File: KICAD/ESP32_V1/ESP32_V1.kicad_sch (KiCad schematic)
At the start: 24 parts

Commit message: Progress ESP32 V1 KiCad PCB design
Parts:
- added J_ADC_Header1: ADC_Header, ESP32_V1:PinHeader_1x08_P2.54mm_Vertical, symbol Connector_Generic:Conn_01x08
- added J_DS2413: OneWire_DS2413_Breakout, Connector_PinSocket_2.54mm:PinSocket_1x04_P2.54mm_Vertical, symbol Connector_Generic:Conn_01x04
- added J_Port_Header1: Port_Header, ESP32_V1:PinHeader_1x08_P2.54mm_Vertical, symbol Connector_Generic:Conn_01x08
- added R11, R12: 4K7, ESP32_V1:R_Axial_DIN0204_L3.6mm_D1.6mm_P2.54mm_Vertical, symbol Device:R
- added SEL_D26: LOOP_B / DS2413_PIOB, ESP32_V1:PinHeader_1x03_P2.54mm_Vertical, symbol Jumper:Jumper_3_Open
- added SEL_D33: DS2413_PIOA / LOOP_A, ESP32_V1:PinHeader_1x03_P2.54mm_Vertical, symbol Jumper:Jumper_3_Open
- added TP1: TestPoint, ESP32_V1:TestPoint_THTPad_D1.5mm_Drill0.7mm, symbol Connector:TestPoint
- C_FB1: footprint (none) -> ESP32_V1:C_Disc_D4.7mm_W2.5mm_P5.00mm
- JP_External_5V1: value LOCAL_LOOP_DEFAULT_OPEN -> Enable_EXT_5V; footprint (none) -> ESP32_V1:PinHeader_1x02_P2.54mm_Vertical
- JP_UART_LOOP2: value LOCAL_LOOP_DEFAULT_OPEN -> Enable_Uart_Loop2; footprint (none) -> ESP32_V1:PinHeader_1x02_P2.54mm_Vertical
- J_AUTO1, J_UART2: footprint (none) -> ESP32_V1:TerminalBlock_Phoenix_MPT-0,5-3-2.54_1x03_P2.54mm_Horizontal
- J_DUT_L1, J_DUT_R1: footprint (none) -> ESP32_V1:PinSocket_1x19_P2.54mm_Vertical
- J_External_PWR1: footprint (none) -> ESP32_V1:TerminalBlock_Phoenix_MPT-0,5-2-2.54_1x02_P2.54mm_Horizontal
- J_FLASH1: footprint (none) -> ESP32_V1:PinSocket_1x06_P2.54mm_Vertical
- J_Grove_I2C1: footprint (none) -> ESP32_V1:Grove_1x04_P2mm(SEEED_110990030)
- J_ONEWIRE1: renamed from J?_OneWire1; footprint (none) -> ESP32_V1:TerminalBlock_Phoenix_MPT-0,5-3-2.54_1x03_P2.54mm_Horizontal
- R1: renamed from R_UART1; footprint (none) -> ESP32_V1:R_Axial_DIN0204_L3.6mm_D1.6mm_P2.54mm_Vertical
- R2: renamed from R_UART2; footprint (none) -> ESP32_V1:R_Axial_DIN0204_L3.6mm_D1.6mm_P2.54mm_Vertical
- R3: renamed from R_LOOP_A1; footprint (none) -> ESP32_V1:R_Axial_DIN0204_L3.6mm_D1.6mm_P2.54mm_Vertical
- R4: renamed from R_LOOP_B1; footprint (none) -> ESP32_V1:R_Axial_DIN0204_L3.6mm_D1.6mm_P2.54mm_Vertical
- R5: renamed from R_PWM1; footprint (none) -> ESP32_V1:R_Axial_DIN0204_L3.6mm_D1.6mm_P2.54mm_Vertical
- R6: renamed from R_1W1; value 4k7 -> 2K2; footprint (none) -> ESP32_V1:R_Axial_DIN0204_L3.6mm_D1.6mm_P2.54mm_Vertical
- R7: renamed from R_I2C_FB1; footprint (none) -> ESP32_V1:R_Axial_DIN0204_L3.6mm_D1.6mm_P2.54mm_Vertical
- R8: renamed from R_I2C_LOOP1; footprint (none) -> ESP32_V1:R_Axial_DIN0204_L3.6mm_D1.6mm_P2.54mm_Vertical
- SEL_D35: value Jumper_3_Open -> I2C_INT / UART1; footprint (none) -> ESP32_V1:PinHeader_1x03_P2.54mm_Vertical
- U_1W1, U_1W2: footprint (none) -> ESP32_V1:TO-92_Inline
- U_I2C1: footprint (none) -> ESP32_V1:DIP-18_W7.62mm_Socket
- U_SPI1: footprint (none) -> ESP32_V1:DIP-16_W7.62mm_Socket
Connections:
- net 3V3: now also R11.1, R12.1
- net D13_ONEWIRE_DQ: now also J_DS2413.3 (Pin_3)
- net D25_LOOP_B_OUT: now also SEL_D26.1 (A); no longer R4.2
- net D26_LOOP_B_IN: now also R4.2; no longer R4.1
- net D32_LOOP_A_OUT: now also SEL_D33.1 (A); no longer R3.2
- net D33_LOOP_A_IN: now also R3.2; no longer R3.1
- net D34_ADC_IN: now also J_ADC_Header1.1 (Pin_1), TP1.1
- net GND: now also J_DS2413.4 (Pin_4)
- net I2C_GP0: now also J_Port_Header1.1 (Pin_1)
- net I2C_GP1: now also J_Port_Header1.2 (Pin_2)
- net I2C_GP2: now also J_Port_Header1.3 (Pin_3)
- net at U_I2C1.13 (GP3): now also J_Port_Header1.4 (Pin_4)
- net at U_I2C1.14 (GP4): now also J_Port_Header1.5 (Pin_5)
- net at U_I2C1.15 (GP5): now also J_Port_Header1.6 (Pin_6)
- net at U_I2C1.16 (GP6): now also J_Port_Header1.7 (Pin_7)
- net at U_I2C1.17 (GP7): now also J_Port_Header1.8 (Pin_8)
- net at U_SPI1.2 (CH1): now also J_ADC_Header1.2 (Pin_2)
- net at U_SPI1.3 (CH2): now also J_ADC_Header1.3 (Pin_3)
- net at U_SPI1.4 (CH3): now also J_ADC_Header1.4 (Pin_4)
- net at U_SPI1.5 (CH4): now also J_ADC_Header1.5 (Pin_5)
- net at U_SPI1.6 (CH5): now also J_ADC_Header1.6 (Pin_6)
- net at U_SPI1.7 (CH6): now also J_ADC_Header1.7 (Pin_7)
- net at U_SPI1.8 (CH7): now also J_ADC_Header1.8 (Pin_8)
- new net: R3.1, SEL_D33.2 (C)
- new net: R4.1, SEL_D26.2 (C)
- new net DS2413_PIOA: J_DS2413.2 (Pin_2), R11.2, SEL_D33.3 (B)
- new net DS2413_PIOB: J_DS2413.1 (Pin_1), R12.2, SEL_D26.3 (B)
- no-connect marks 24 -> 12
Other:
- note added: "DS2413_PIOA ── R? 470R ── DS2413_FB_A DS2413_PIOB ── R? 470R ── DS2413_FB_B"
- note added: "I2C MCP23008 + GROVE I2C Extension"
- note added: "I’d retain R3 and R4, relocate them to the common paths, and remove R9 and R10."
- note added: "LoopBack Test Selectors - GPIO LOOPBACKS / DS2413 Breakout"
- note added: "ONEWIRE - DS2413 Breakout"
- note added: "ONEWIRE - TWO DS18B20 + External Option"
- note added: "R? 4.7k: 3V3 → DS2413_PIOA R? 4.7k: 3V3 → DS2413_PIOB"
- note added: "R_DS2413_PUA R_DS2413_PUB"
- note removed: "GPIO LOOPBACKS"
- note removed: "I2C MCP23008 (0x20)"
- note removed: "ONEWIRE - TWO POWERED DEVICES"
- moved on the sheet: C_FB1, J_FLASH1, J_Grove_I2C1, J_ONEWIRE1, R3, R4, R5, R6, R7, R8, U_1W1, U_1W2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

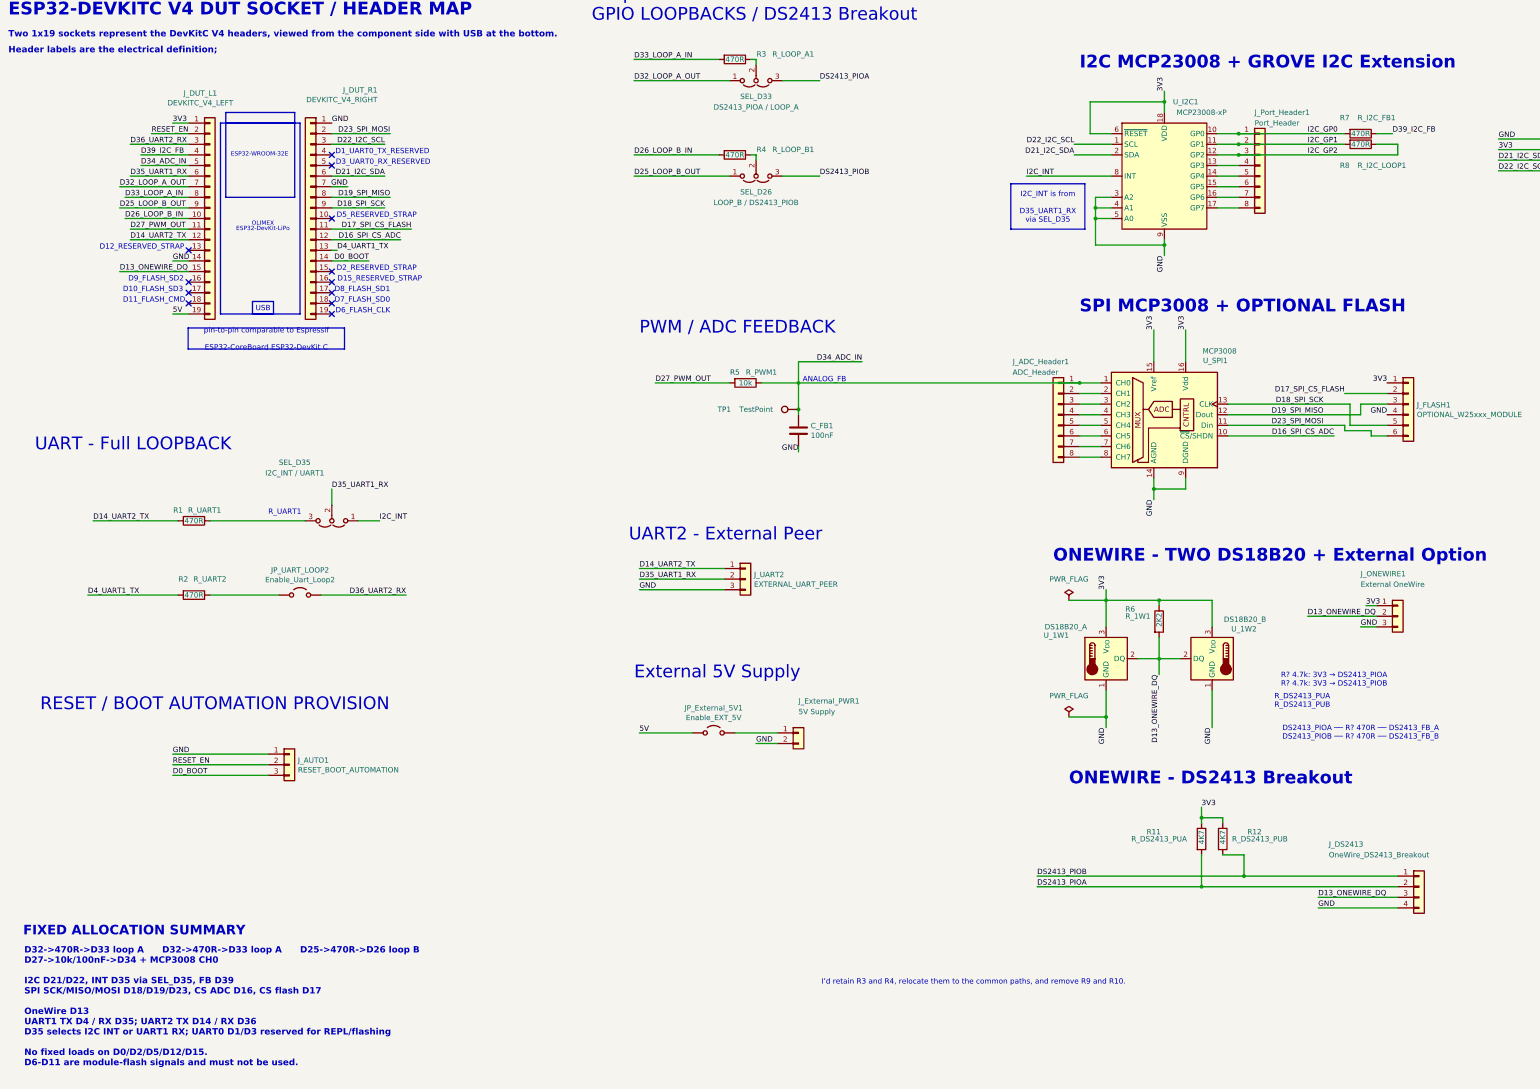
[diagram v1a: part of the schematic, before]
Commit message: Finalize ESP32_V1 v1.0 build documentation
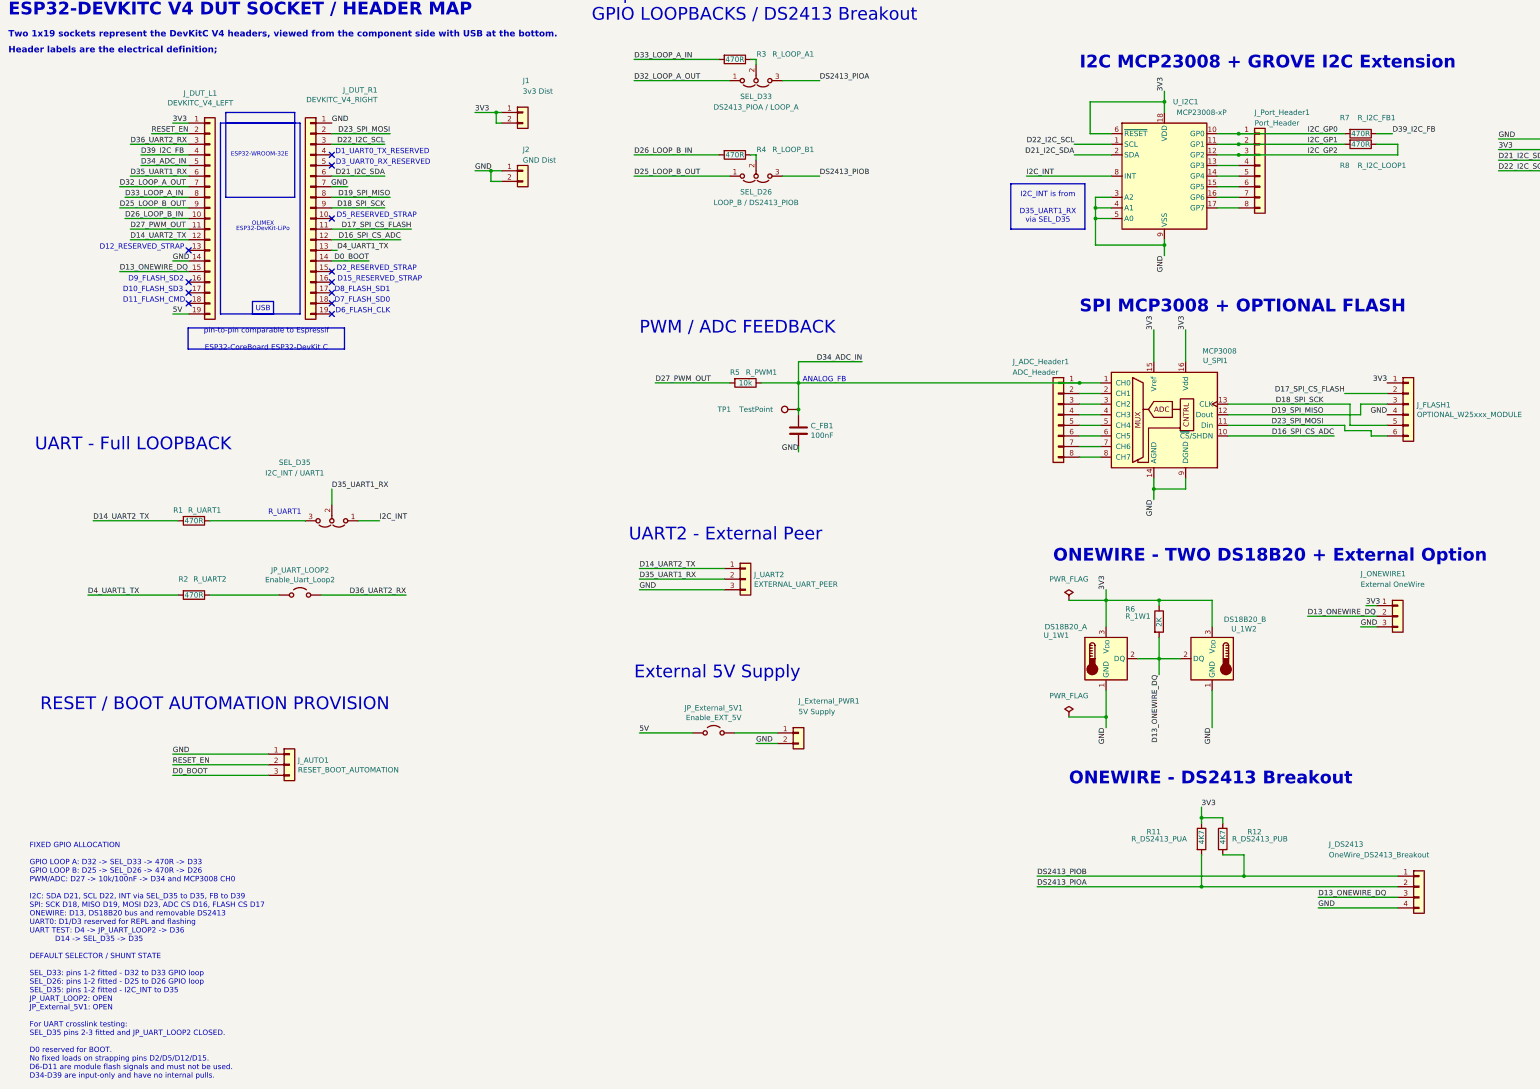
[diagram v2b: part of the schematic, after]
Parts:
- added J1: 3v3 Dist, ESP32_V1:PinHeader_1x02_P2.54mm_Vertical, symbol Connector_Generic:Conn_01x02
- added J2: GND Dist, ESP32_V1:PinHeader_1x02_P2.54mm_Vertical, symbol Connector_Generic:Conn_01x02
- R6: value 2K2 -> 2K
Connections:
- net 3V3: now also J1.1 (Pin_1), J1.2 (Pin_2)
- net GND: now also J2.1 (Pin_1), J2.2 (Pin_2)
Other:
- note added: "FIXED GPIO ALLOCATION GPIO LOOP A: D32 -> SEL_D33 -> 470R -> D33 GPIO LOOP B: D25 -> SEL_D26 -> 470R -> D26 PWM/ADC: D27 -> 10k/100nF -> D34 and MCP3008 CH0 I2C: SDA D21, SCL D22, INT via SEL_D35 to D35, FB to D39 SPI: SCK D18, MISO D19, MOSI D23, ADC CS D16, FLASH CS D17 ONEWIRE: D13, DS18B20 bus and removable DS2413 UART0: D1/D3 reserved for REPL and flashing UART TEST: D4 -> JP_UART_LOOP2 -> D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"
- note removed: "D32->470R->D33 loop A D32->470R->D33 loop A D25->470R->D26 loop B D27->10k/100nF->D34 + MCP3008 CH0 I2C D21/D22, INT D35 via SEL_D35, FB D39 SPI SCK/MISO/MOSI D18/D19/D23, CS ADC D16, CS flash D17 OneWire D13 UART1 TX D4 / RX D35; UART2 TX D14 / RX D36 D35 selects I2C INT or UART1 RX; UART0 D1/D3 reserved for REPL/flashing No fixed loads on D0/D2/D5/D12/D15. D6-D11 are module-flash signals and mu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"
- note removed: "DS2413_PIOA ── R? 470R ── DS2413_FB_A DS2413_PIOB ── R? 470R ── DS2413_FB_B"
- note removed: "FIXED ALLOCATION SUMMARY"
- note removed: "I’d retain R3 and R4, relocate them to the common paths, and remove R9 and R10."
- note removed: "R? 4.7k: 3V3 → DS2413_PIOA R? 4.7k: 3V3 → DS2413_PIOB"
- note removed: "R_DS2413_PUA R_DS2413_PUB"
